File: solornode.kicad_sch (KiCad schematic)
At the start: 84 parts, among them J1 Conn_01x06, J2 Conn_01x02, J3 Conn_01x02, J4 Conn_01x02, Q1 Q_NMOS_GDS, Q4 Q_PNP_BCE, Q5 Q_NPN_BCE, SW1 SW_Push, U1 LM358, U2 OC5864, U3 PY32F003F1xUx, U4 MAX485E, U5 SGM2033-3.3

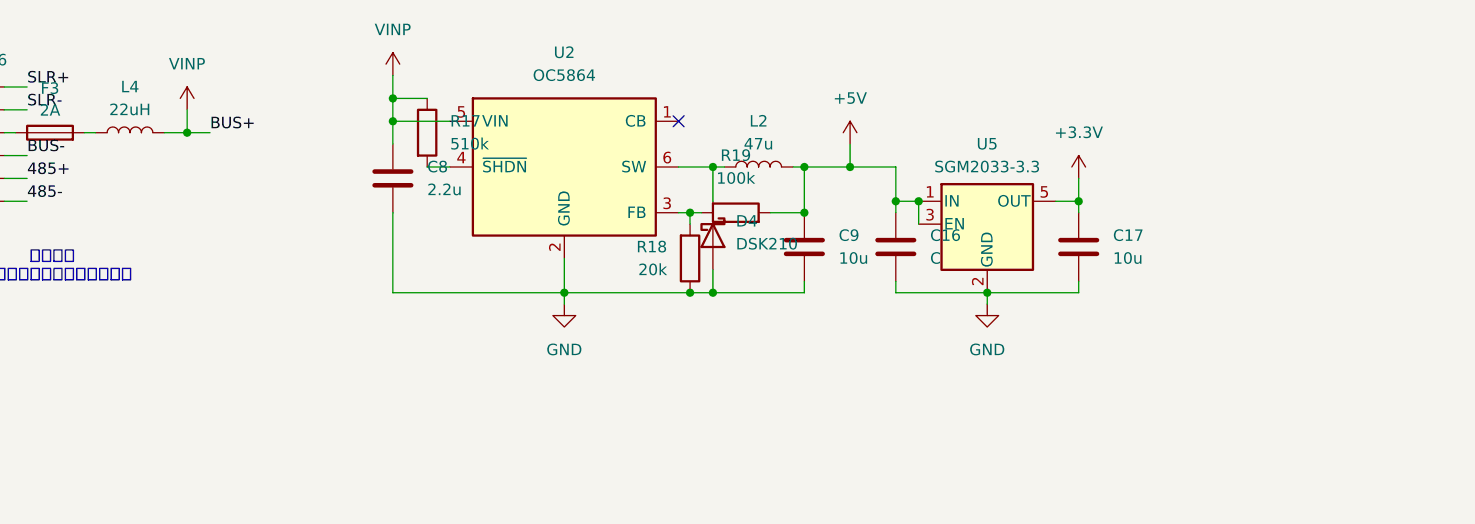
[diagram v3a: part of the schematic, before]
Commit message: DCDC输入前使用二极管切换电源
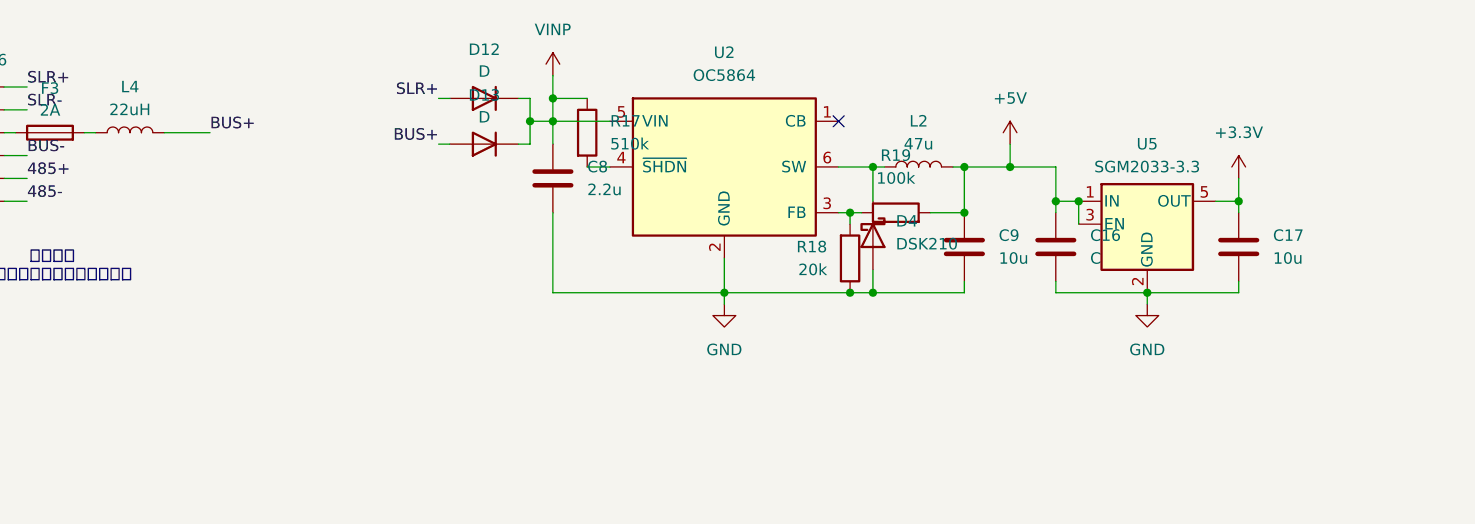
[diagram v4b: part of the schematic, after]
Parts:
- added D12, D13: D, Diode_SMD:D_SOD-123F, symbol Device:D
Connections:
- net SLR+: now also D12.2 (A)
- net VINP: now also D12.1 (K), D13.1 (K); no longer C3.1, C4.1, D1.1 (K), L4.2, R15.1
- new net BUS+: C3.1, C4.1, D1.1 (K), D13.2 (A), L4.2, R15.1
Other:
- moved on the sheet: C16, C17, C8, C9, D4, L2, R17, R18, R19, U2, U5

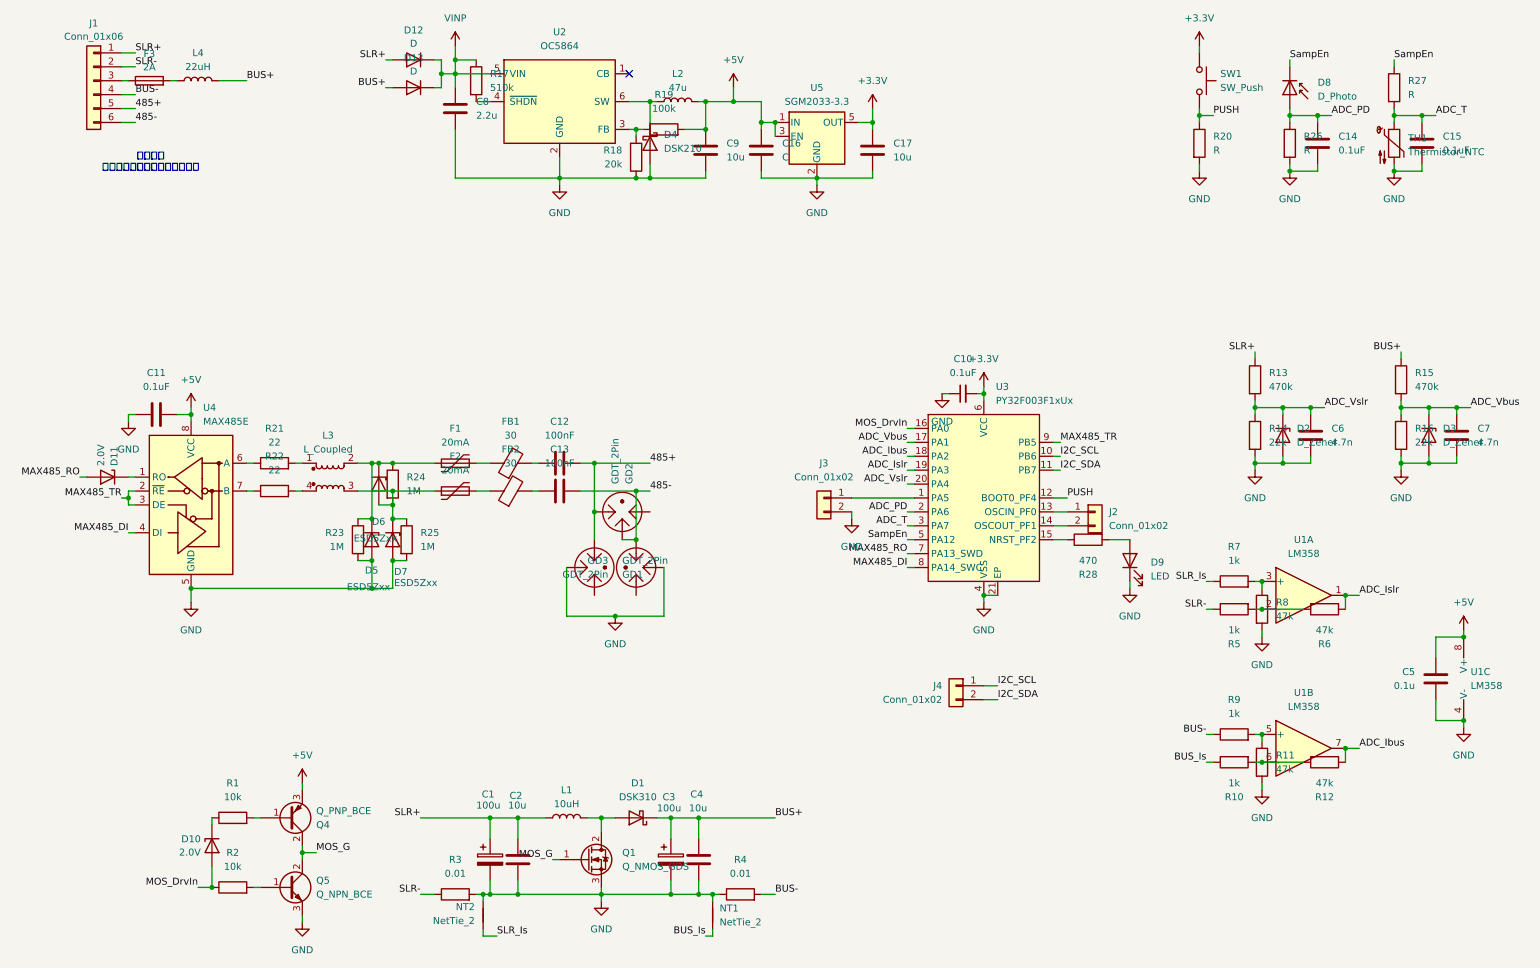
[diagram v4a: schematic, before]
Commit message: 修改元器件参数
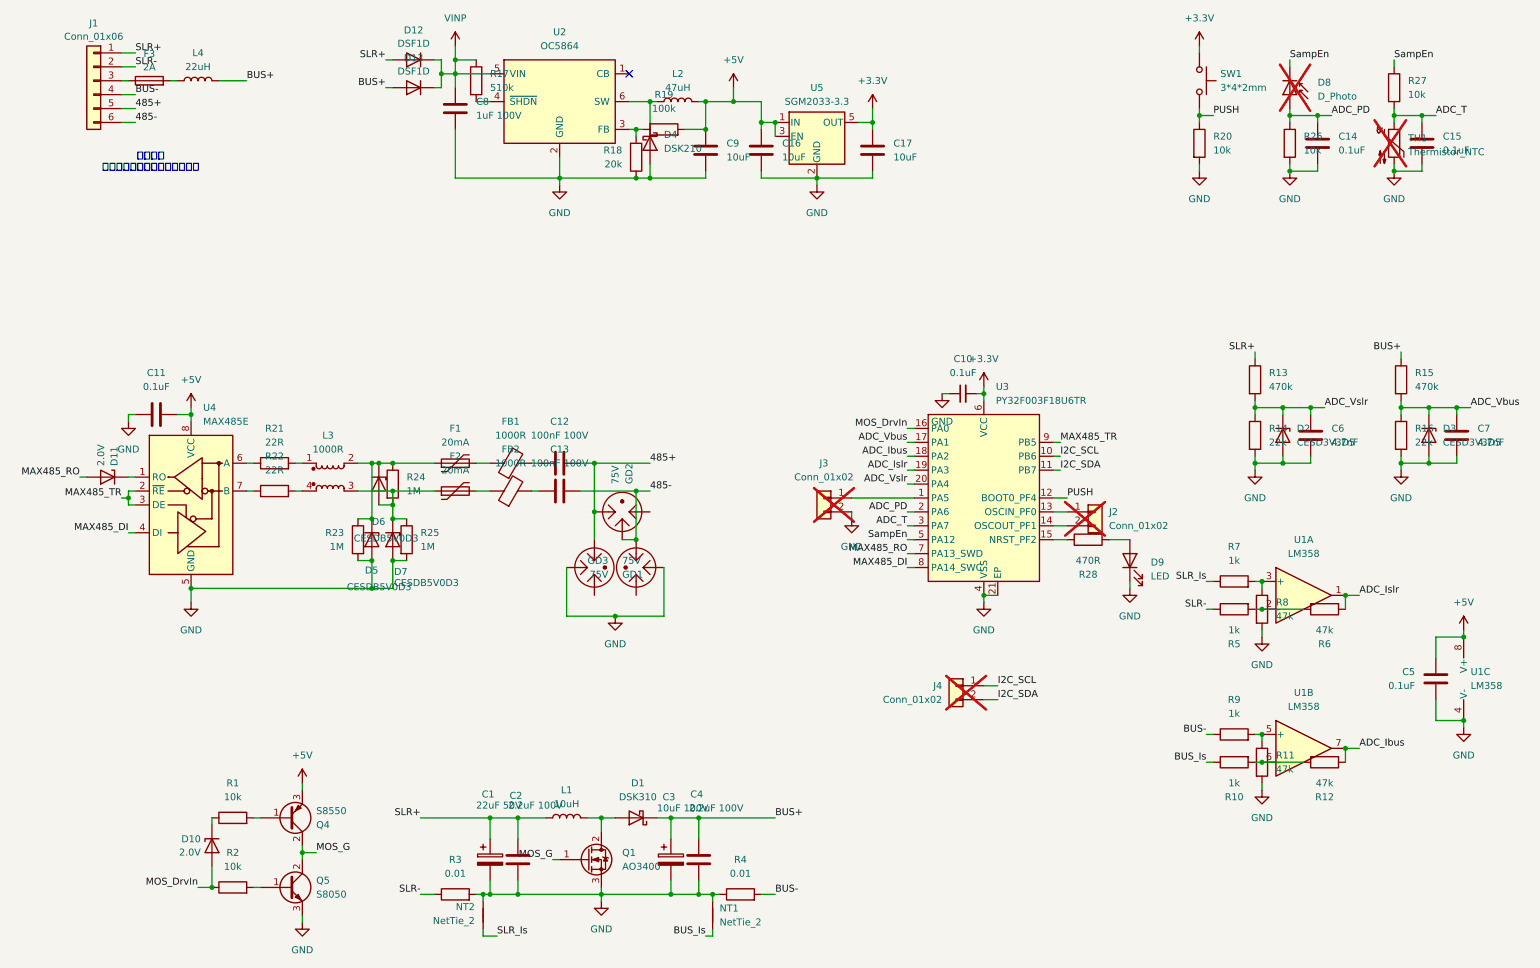
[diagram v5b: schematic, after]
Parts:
- C1: value 100u -> 22uF 50V
- C12, C13: value 100nF -> 100nF 100V
- C16: value C -> 10uF
- C17, C9: value 10u -> 10uF
- C2, C4: value 10u -> 2.2uF 100V
- C3: value 100u -> 10uF 100V
- C5: value 0.1u -> 0.1uF
- C6, C7: value 4.7n -> 4.7nF
- C8: value 2.2u -> 1uF 100V
- D12, D13: value D -> DSF1D
- D2, D3: value D_Zener -> CESD3V3D5
- D5, D6, D7: value ESD5Zxx -> CESDB5V0D3
- D8, J2, J3, J4, TH1: now not fitted
- FB1, FB2: value 30 -> 1000R
- GD1, GD2, GD3: value GDT_2Pin -> 75V
- L2: value 47u -> 47uH
- L3: value L_Coupled -> 1000R
- Q1: value Q_NMOS_GDS -> AO3400
- Q4: value Q_PNP_BCE -> S8550
- Q5: value Q_NPN_BCE -> S8050
- R20, R26, R27: value R -> 10k
- R21, R22: value 22 -> 22R
- R28: value 470 -> 470R
- SW1: value SW_Push -> 3*4*2mm
- U3: value PY32F003F1xUx -> PY32F003F18U6TR
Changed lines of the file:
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@@
 			)
 		)
-		(property "Value" "D_Zener"
+		(property "Value" "CESD3V3D5"
 			(at 240.03 95.2499 90)
 			(effects
@@
 			)
 		)
-		(property "Value" "10u"
+		(property "Value" "2.2uF 100V"
 			(at 129.032 162.052 0)
 			(effects
@@
 			)
 		)
-		(property "Value" "D"
+		(property "Value" "DSF1D"
 			(at 78.74 22.4098 0)
 			(effects
@@
 			)
 		)
-		(property "Value" "L_Coupled"
+		(property "Value" "1000R"
 			(at 63.119 96.52 0)
 			(effects
@@
 			)
 		)
-		(property "Value" "100nF"
+		(property "Value" "100nF 100V"
 			(at 105.41 99.06 90)
 			(effects
@@
 			)
 		)
-		(property "Value" "10u"
+		(property "Value" "10uF"
 			(at 135.89 43.1799 0)
 			(effects
@@
 			)
 		)
-		(property "Value" "30"
+		(property "Value" "1000R"
 			(at 96.4692 93.98 90)
 			(effects
@@
 			)
 		)
-		(property "Value" "Q_NMOS_GDS"
+		(property "Value" "AO3400"
 			(at 116.84 172.7199 0)
 			(effects
@@
 			)
 		)
-		(property "Value" "GDT_2Pin"
+		(property "Value" "75V"
 			(at 115.5701 102.87 0)
 			(effects
@@
 		(in_bom yes)
 		(on_board yes)
-		(dnp no)
+		(dnp yes)
 		(fields_autoplaced yes)
 		(property "Reference" "TH1"
@@
 			)
 		)
-		(property "Value" "Q_PNP_BCE"
+		(property "Value" "S8550"
 			(at 60.96 162.5601 0)
 			(effects
@@
 			)
 		)
-		(property "Value" "22"
+		(property "Value" "22R"
 			(at 53.34 95.25 90)
 			(effects
@@
 			)
 		)
-		(property "Value" "GDT_2Pin"
+		(property "Value" "75V"
 			(at 114.3 119.3799 0)
 			(effects
@@
 			)
 		)
-		(property "Value" "R"
+		(property "Value" "10k"
 			(at 260.35 31.7499 0)
 			(effects
@@
 			)
 		)
-		(property "Value" "D_Zener"
+		(property "Value" "CESD3V3D5"
 			(at 266.7 95.2499 90)
 			(effects
@@
 			)
 		)
-		(property "Datasheet" "http://www.ti.com/lit/ds/symlink/tlv700.pdf"
+		(property "Datasheet" "https://www.sg-micro.com/cn/product/SGM2033"
 			(at 152.4 38.1 0)
 			(effects
@@
 			)
 		)
-		(property "Value" "C"
+		(property "Value" "10uF"
 			(at 146.05 43.1799 0)
 			(effects
@@
 			)
 		)
-		(property "Value" "ESD5Zxx"
+		(property "Value" "CESDB5V0D3"
 			(at 67.818 112.776 90)
 			(effects
@@
 			)
 		)
-		(property "Datasheet" "https://www.onsemi.com/pdf/datasheet/esd5z2.5t1-d.pdf"
+		(property "Datasheet" ""
 			(at 72.39 102.87 0)
 			(effects
@@
 			)
 		)
-		(property "Value" "470"
+		(property "Value" "470R"
 			(at 201.93 116.84 90)
 			(effects
@@
 			)
 		)
-		(property "Value" "10u"
+		(property "Value" "10uF"
 			(at 166.37 43.1799 0)
 			(effects
@@
 		(in_bom yes)
 		(on_board yes)
-		(dnp no)
+		(dnp yes)
 		(fields_autoplaced yes)
 		(property "Reference" "J2"
@@
 			)
 		)
-		(property "Value" "2.2u"
+		(property "Value" "1uF 100V"
 			(at 90.17 35.5599 0)
 			(effects
@@
 			)
 		)
-		(property "Value" "Q_NPN_BCE"
+		(property "Value" "S8050"
 			(at 60.96 177.7999 0)
 			(effects
@@
 			)
 		)
-		(property "Value" "SW_Push"
+		(property "Value" "3*4*2mm"
 			(at 226.06 30.4799 90)
 			(effects
@@
 			)
 		)
-		(property "Value" "ESD5Zxx"
+		(property "Value" "CESDB5V0D3"
 			(at 66.548 121.666 90)
 			(effects
@@
 			)
 		)
-		(property "Datasheet" "https://www.onsemi.com/pdf/datasheet/esd5z2.5t1-d.pdf"
+		(property "Datasheet" ""
 			(at 71.12 113.03 0)
 			(effects
@@
 		(in_bom yes)
 		(on_board yes)
-		(dnp no)
+		(dnp yes)
 		(fields_autoplaced yes)
 		(property "Reference" "D8"
@@
 			)
 		)
-		(property "Value" "4.7n"
+		(property "Value" "4.7nF"
 			(at 246.38 95.2499 0)
 			(effects
@@
 		(in_bom yes)
 		(on_board yes)
-		(dnp no)
+		(dnp yes)
 		(fields_autoplaced yes)
 		(property "Reference" "J3"
@@
 			)
 		)
-		(property "Value" "100nF"
+		(property "Value" "100nF 100V"
 			(at 105.41 93.98 90)
 			(effects
@@
 			)
 		)
-		(property "Value" "D"
+		(property "Value" "DSF1D"
 			(at 78.74 27.4898 0)
 			(effects
@@
 		(in_bom yes)
 		(on_board yes)
-		(dnp no)
+		(dnp yes)
 		(property "Reference" "J4"
 			(at 175.26 139.6999 0)
@@
 			)
 		)
-		(property "Value" "30"
+		(property "Value" "1000R"
 			(at 96.4692 99.06 90)
 			(effects
@@
 			)
 		)
-		(property "Value" "ESD5Zxx"
+		(property "Value" "CESDB5V0D3"
 			(at 75.184 120.904 90)
 			(effects
@@
 			)
 		)
-		(property "Datasheet" "https://www.onsemi.com/pdf/datasheet/esd5z2.5t1-d.pdf"
+		(property "Datasheet" ""
 			(at 74.93 113.03 0)
 			(effects
@@
 			)
 		)
-		(property "Value" "R"
+		(property "Value" "10k"
 			(at 241.3 41.9099 0)
 			(effects
@@
 			)
 		)
-		(property "Value" "100u"
+		(property "Value" "10uF 100V"
 			(at 123.19 162.052 0)
 			(effects
@@
 			)
 		)
-		(property "Value" "4.7n"
+		(property "Value" "4.7nF"
 			(at 273.05 95.2499 0)
 			(effects
@@
 			)
 		)
-		(property "Value" "0.1u"
+		(property "Value" "0.1uF"
 			(at 261.62 139.6999 0)
 			(effects
@@
 			)
 		)
-		(property "Datasheet" "https://www.ti.com/lit/ds/symlink/lv2862.pdf"
+		(property "Datasheet" "http://ocxsemi.com/uploads/soft/20220426/1650943254.pdf"
 			(at 95.25 21.59 0)
 			(effects
@@
 			)
 		)
-		(property "Value" "100u"
+		(property "Value" "22uF 50V"
 			(at 90.17 161.544 0)
 			(effects
@@
 			)
 		)
-		(property "Value" "GDT_2Pin"
+		(property "Value" "75V"
 			(at 116.84 116.8401 0)
 			(effects
@@
 			)
 		)
-		(property "Value" "10u"
+		(property "Value" "2.2uF 100V"
 			(at 96.012 161.544 0)
 			(effects
@@
 			)
 		)
-		(property "Value" "22"
+		(property "Value" "22R"
 			(at 53.34 100.33 90)
 			(effects
@@
 			)
 		)
-		(property "Value" "R"
+		(property "Value" "10k"
 			(at 224.79 41.9099 0)
 			(effects
@@
 			)
 		)
-		(property "Value" "PY32F003F1xUx"
+		(property "Value" "PY32F003F18U6TR"
 			(at 185.0741 87.63 0)
 			(effects
@@
 			)
 		)
-		(property "Datasheet" ""
+		(property "Datasheet" "https://www.puyasemi.com/download_path/%E6%95%B0%E6%8D%AE%E6%89%8B%E5%86%8C/MCU%20%E5%BE%AE%E5%A4%84%E7%90%86%E5%99%A8/PY32F003%E7%B3%BB%E5%88%97%E6%95%B0%E6%8D%AE%E6%89%8B%E5%86%8C_V2.7.pdf"
 			(at 182.88 104.14 0)
 			(effects
@@
 			)
 		)
-		(property "Value" "47u"
+		(property "Value" "47uH"
 			(at 127 30.48 90)
 			(effects

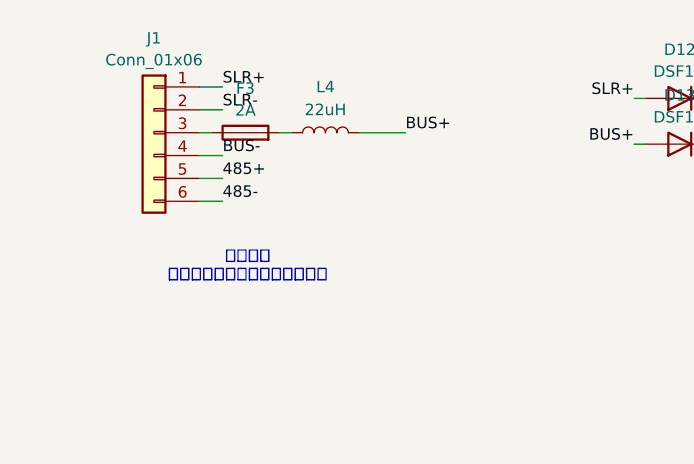
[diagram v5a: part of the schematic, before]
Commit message: 移除电源总线滤波电感
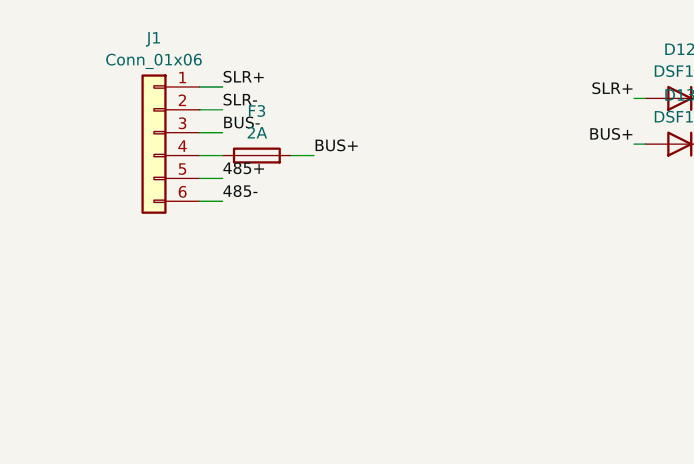
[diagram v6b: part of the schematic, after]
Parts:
- removed L4: 22uH, Inductor_SMD:L_APV_APH0630, symbol Device:L
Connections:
- net BUS+: now also F3.2
- net BUS-: now also J1.3 (Pin_3); no longer J1.4 (Pin_4)
- net at F3.1: now also J1.4 (Pin_4); no longer J1.3 (Pin_3)
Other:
- note removed: "电感可选 用于电源线和信号线共用时隔离"
- moved on the sheet: F3
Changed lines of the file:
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@@
 	(wire
 		(pts
-			(xy 34.29 29.21) (xy 35.56 29.21)
+			(xy 35.56 31.75) (xy 38.1 31.75)
 		)
 		(stroke
@@
 	(wire
 		(pts
+			(xy 25.4 31.75) (xy 27.94 31.75)
+		)
+		(stroke
+			(width 0)
+			(type default)
+		)
+	)
+	(wire
+		(pts
 			(xy 168.91 92.71) (xy 170.18 92.71)
 		)
@@
 	(wire
 		(pts
-			(xy 27.94 31.75) (xy 25.4 31.75)
-		)
-		(stroke
-			(width 0)
-			(type default)
-		)
-	)
-	(wire
-		(pts
 			(xy 248.92 123.19) (xy 251.46 123.19)
 		)
@@
 	(wire
 		(pts
+			(xy 25.4 29.21) (xy 27.94 29.21)
+		)
+		(stroke
+			(width 0)
+			(type default)
+		)
+	)
+	(wire
+		(pts
 			(xy 144.78 36.83) (xy 144.78 39.37)
 		)
@@
 	(wire
 		(pts
-			(xy 26.67 29.21) (xy 25.4 29.21)
-		)
-		(stroke
-			(width 0)
-			(type default)
-		)
-	)
-	(wire
-		(pts
 			(xy 121.92 46.99) (xy 119.38 46.99)
 		)
@@
 	(wire
 		(pts
-			(xy 43.18 29.21) (xy 48.26 29.21)
-		)
-		(stroke
-			(width 0)
-			(type default)
-		)
-	)
-	(wire
-		(pts
 			(xy 270.51 129.54) (xy 270.51 130.81)
 		)
@@
 		)
 	)
-	(text "电感可选\n用于电源线和信号线共用时隔离"
-		(exclude_from_sim no)
-		(at 30.734 44.196 0)
-		(effects
-			(font
-				(size 1.27 1.27)
-			)
-		)
-	)
 	(label "MOS_G"
 		(at 104.14 171.45 180)
@@
 	)
 	(label "BUS-"
-		(at 27.94 31.75 0)
+		(at 27.94 29.21 0)
 		(effects
 			(font
@@
 	)
 	(label "BUS+"
-		(at 48.26 29.21 0)
+		(at 38.1 31.75 0)
 		(effects
 			(font
@@
 	(symbol
 		(lib_id "Device:Fuse")
-		(at 30.48 29.21 90)
+		(at 31.75 31.75 90)
 		(unit 1)
 		(exclude_from_sim no)
@@
 		(fields_autoplaced yes)
 		(property "Reference" "F3"
-			(at 30.48 24.3035 90)
+			(at 31.75 26.8435 90)
 			(effects
 				(font
@@
 		)
 		(property "Value" "2A"
-			(at 30.48 26.7278 90)
+			(at 31.75 29.2678 90)
 			(effects
 				(font
@@
 		)
 		(property "Footprint" "Fuse:Fuse_1206_3216Metric"
-			(at 30.48 30.988 90)
+			(at 31.75 33.528 90)
 			(effects
 				(font
@@
 		)
 		(property "Datasheet" "~"
-			(at 30.48 29.21 0)
+			(at 31.75 31.75 0)
 			(effects
 				(font
@@
 		)
 		(property "Description" "Fuse"
-			(at 30.48 29.21 0)
+			(at 31.75 31.75 0)
 			(effects
 				(font
@@
 					(unit 1)
 				)
-			)
-		)
-	)
-	(symbol
-		(lib_id "Device:L")
-		(at 39.37 29.21 90)
-		(unit 1)
-		(exclude_from_sim no)
-		(in_bom yes)
-		(on_board yes)
-		(dnp no)
-		(fields_autoplaced yes)
-		(property "Reference" "L4"
-			(at 39.37 24.13 90)
-			(effects
-				(font
-					(size 1.27 1.27)
-				)
-			)
-		)
-		(property "Value" "22uH"
-			(at 39.37 26.67 90)
-			(effects
-				(font
-					(size 1.27 1.27)
-				)
-			)
-		)
-		(property "Footprint" "Inductor_SMD:L_APV_APH0630"
-			(at 39.37 29.21 0)
-			(effects
-				(font
-					(size 1.27 1.27)
-				)
-				(hide yes)
-			)
-		)
-		(property "Datasheet" "~"
-			(at 39.37 29.21 0)
-			(effects
-				(font
-					(size 1.27 1.27)
-				)
-				(hide yes)
-			)
-		)
-		(property "Description" "Inductor"
-			(at 39.37 29.21 0)
-			(effects
-				(font
-					(size 1.27 1.27)
-				)
-				(hide yes)
-			)
-		)
-		(property "Sim.Device" ""
-			(at 39.37 29.21 0)
-			(effects
-				(font
-					(size 1.27 1.27)
-				)
-				(hide yes)
-			)
-		)
-		(property "Sim.Pins" ""
-			(at 39.37 29.21 0)
-			(effects
-				(font
-					(size 1.27 1.27)
-				)
-				(hide yes)
-			)
-		)
-		(property "Sim.Type" ""
-			(at 39.37 29.21 0)
-			(effects
-				(font
-					(size 1.27 1.27)
-				)
-				(hide yes)
-			)
-		)
-		(pin "1"
-		)
-		(pin "2"
-		)
-		(instances
-			(project "solornode"
-				(path "/4bca4b2b-dcb0-465d-ab23-8d5d35a41dfe"
-					(reference "L4")
-					(unit 1)
-				)
